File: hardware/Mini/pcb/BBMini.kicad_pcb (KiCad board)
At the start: 2 copper layers, 122 x 88 mm, 31 parts, among them J1 Schurter_CMF1, J2 Display, SW1 SW_Push, U1 ESP8266-12E_NodeMCU_Lolin, U2 MCP3208

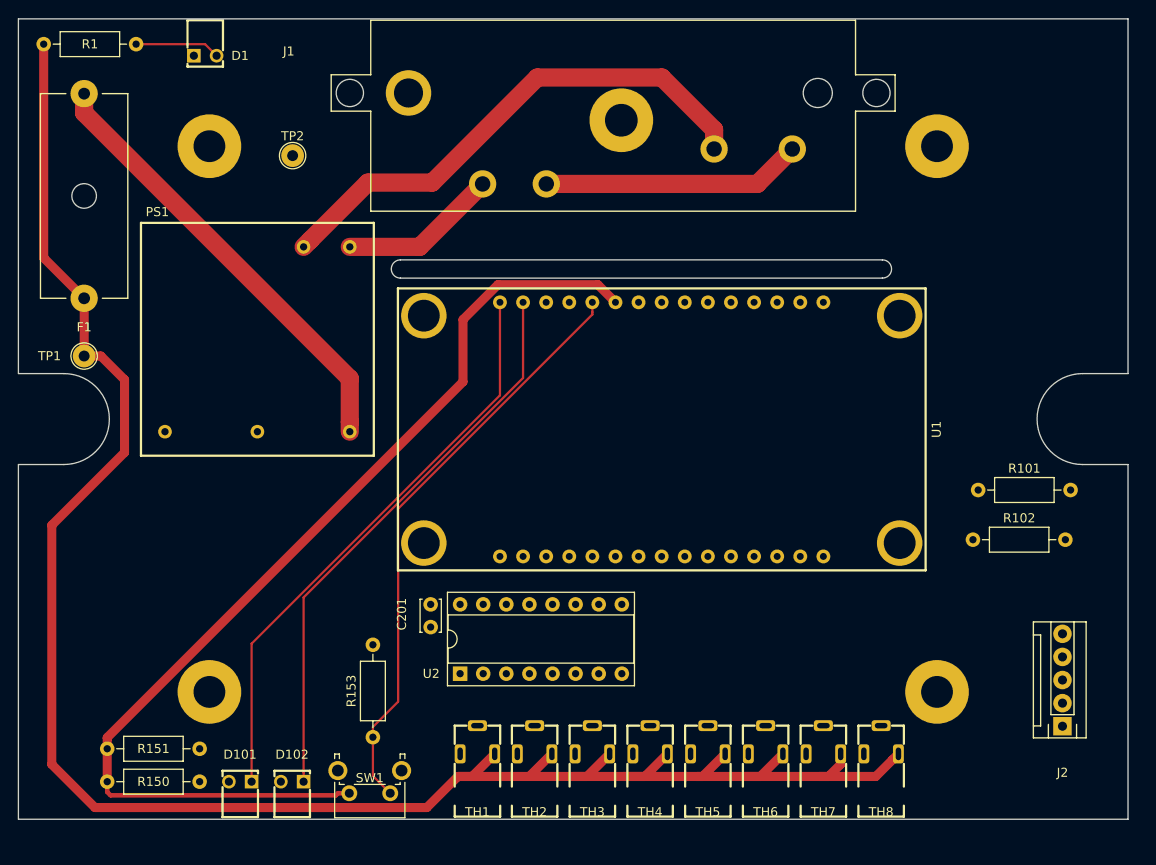
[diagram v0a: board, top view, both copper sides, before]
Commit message: feat: General PCB improvements
add Mini PCB (needs to be redone for RM2015L

Issue #14
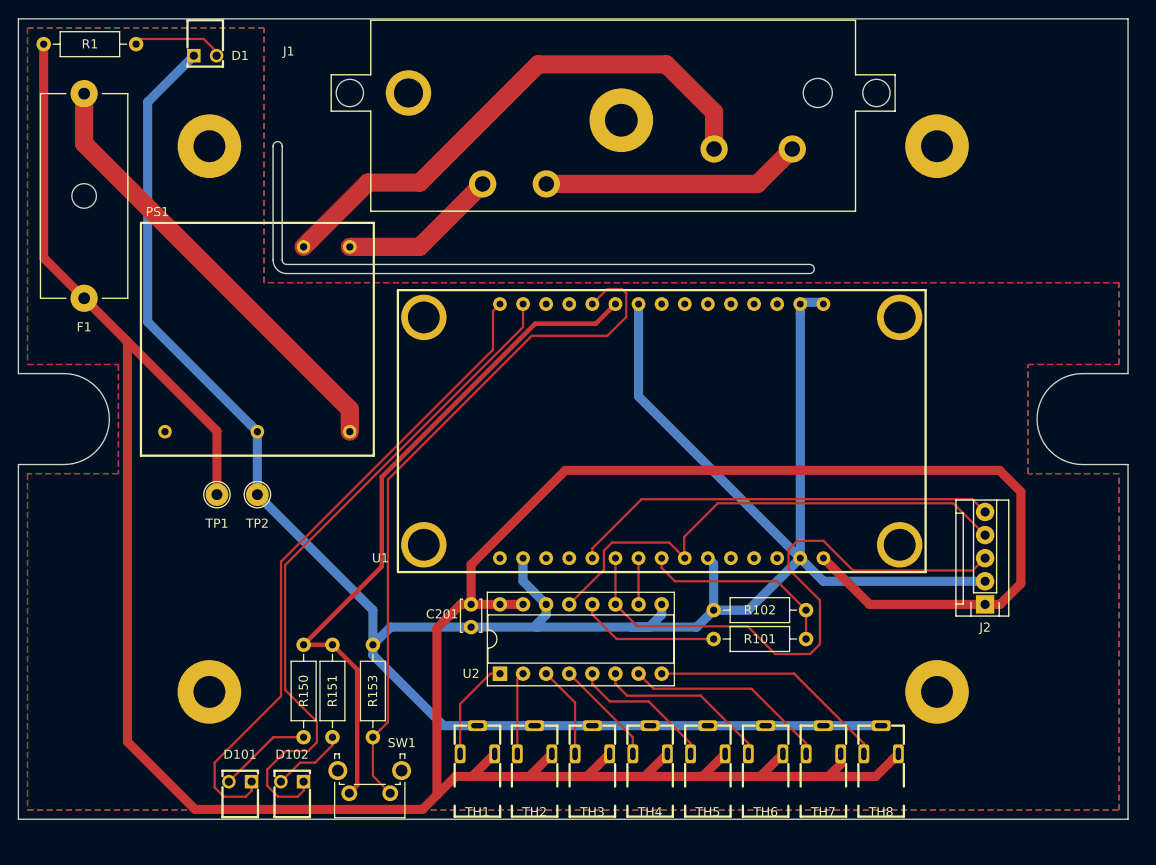
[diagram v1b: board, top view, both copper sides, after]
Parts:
- moved TP2 37.5 mm to (41.3, 67.3)
- moved R151 27.3 mm to (49.5, 83.8), turned to 270 degrees
- moved R150 26.3 mm to (46.4, 83.8), turned to 270 degrees
- moved R101 25.0 mm to (101.6, 83.2), turned to 180 degrees
- moved TP1 21.1 mm to (36.8, 67.3)
- moved R102 19.9 mm to (101.6, 80.0), turned to 180 degrees
- moved J2 15.9 mm to (121.3, 79.4)
- moved C201 4.44 mm to (64.8, 79.4)
- moved U2 4.38 mm to (67.9, 87.0)
- moved U1 0.19 mm to (67.9, 60.3)
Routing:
- net GND: track 0.00 -> 295.4 mm
- net +5V: track 217.7 -> 359.3 mm
- net /Analog/Digital/SPI1: track 0.00 -> 66.0 mm
- net /Analog/Digital/SPI3: track 0.00 -> 55.9 mm
- net /Display/SPI5: track 0.00 -> 47.1 mm
- net +3V3: track 114.2 -> 76.6 mm
- net /Analog/Digital/SIGNAL8: track 0.00 -> 26.6 mm
- net /Analog/Digital/SIGNAL7: track 0.00 -> 22.7 mm
- net /ESP8266/MISO: track 0.00 -> 22.0 mm
- net /Analog/Digital/SIGNAL6: track 0.00 -> 19.6 mm
- net /Analog/Digital/SIGNAL5: track 0.00 -> 15.8 mm
- net /Analog/Digital/SPI2: track 0.00 -> 15.6 mm
- net Net-(D102-Pad1): track 62.7 -> 74.7 mm
- net Net-(R153-Pad1): track 64.8 -> 76.8 mm
- net /Analog/Digital/SIGNAL4: track 0.00 -> 11.7 mm
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- added copper zone on F.Cu, net +5V
- added copper zone on B.Cu, net GND
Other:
- outline, holes or cut-outs redrawn
- net class 3V3 added: clearance 0.3, trace_width 0.5, via_dia 0.8, via_drill 0.4
- net class Large: clearance 0.2 -> 0.5
- net class Medium: clearance 0.2 -> 0.4

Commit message: feat: General PCB improvements
reddo with RM2015L pcb

Issue #14
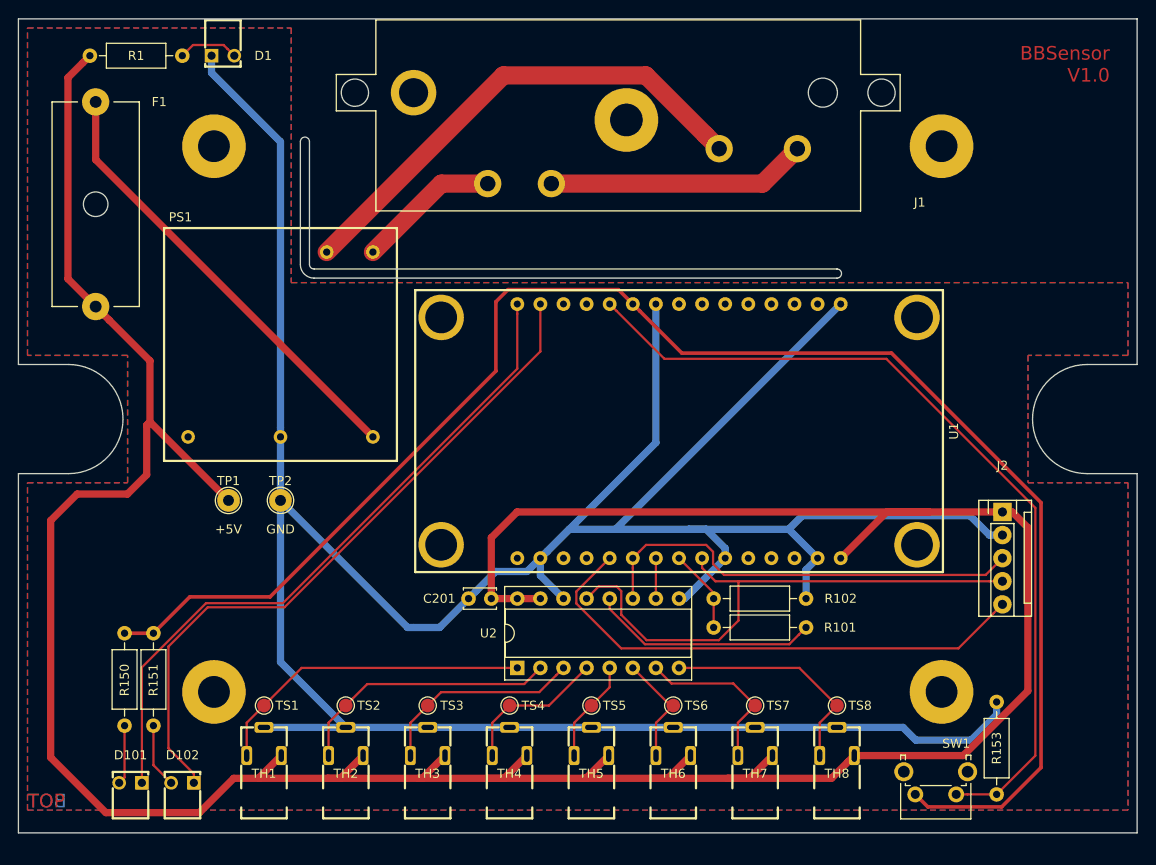
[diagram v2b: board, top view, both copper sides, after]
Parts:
- added TS1: TestPoint, TestPoint:TestPoint_Pad_D1.5mm, F.Cu at (42.0, 90.5)
- added TS2: TestPoint, TestPoint:TestPoint_Pad_D1.5mm, F.Cu at (51.0, 90.5)
- added TS3: TestPoint, TestPoint:TestPoint_Pad_D1.5mm, F.Cu at (60.0, 90.5)
- added TS4: TestPoint, TestPoint:TestPoint_Pad_D1.5mm, F.Cu at (69.0, 90.5)
- added TS5: TestPoint, TestPoint:TestPoint_Pad_D1.5mm, F.Cu at (78.0, 90.5)
- added TS6: TestPoint, TestPoint:TestPoint_Pad_D1.5mm, F.Cu at (87.0, 90.5)
- added TS7: TestPoint, TestPoint:TestPoint_Pad_D1.5mm, F.Cu at (96.0, 90.5)
- added TS8: TestPoint, TestPoint:TestPoint_Pad_D1.5mm, F.Cu at (105.0, 90.5)
- moved R153 68.9 mm to (122.6, 100.3)
- moved SW1 62.2 mm to (118.1, 100.3)
- moved TH1 23.5 mm to (42.0, 102.9)
- moved TH2 20.8 mm to (51.0, 102.9)
- moved R151 19.7 mm to (29.8, 82.5)
- moved R150 19.7 mm to (26.7, 82.5)
- moved TH3 18.1 mm to (60.0, 102.9)
- moved TH4 15.5 mm to (69.0, 102.9)
- moved TH5 12.8 mm to (78.0, 102.9)
- moved D101 12.1 mm to (27.3, 103.0)
- moved D102 12.1 mm to (33.0, 103.0)
- moved J2 10.3 mm to (123.2, 69.2), turned to 0 degrees
- moved R102 10.2 mm to (91.4, 78.7), turned to 0 degrees
- moved R101 10.2 mm to (91.4, 81.9), turned to 0 degrees
- moved TH6 10.2 mm to (87.0, 102.9)
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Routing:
- net +3V3: track 76.6 -> 175.9 mm
- net GND: track 295.4 -> 350.9 mm
- net /Analog/Digital/SIGNAL1: track 11.2 -> 35.9 mm
- net /Analog/Digital/SIGNAL2: track 9.08 -> 29.4 mm
- net /Analog/Digital/SPI1: track 66.0 -> 48.6 mm
- net Net-(R153-Pad1): track 76.8 -> 93.8 mm
- net /ESP8266/MISO: track 22.0 -> 9.20 mm
- net /Analog/Digital/SIGNAL3: track 10.1 -> 22.9 mm
- net /Display/SPI5: track 47.1 -> 57.4 mm
- net /Analog/Digital/SPI2: track 15.6 -> 25.1 mm
- net /Analog/Digital/SIGNAL6: track 19.6 -> 12.5 mm
- net +5V: track 359.3 -> 353.2 mm
- net /Analog/Digital/SPI3: track 55.9 -> 61.1 mm
- net Net-(J1-Pad1): track 59.7 -> 54.5 mm
- net /Analog/Digital/SIGNAL4: track 11.7 -> 16.5 mm
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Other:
- board size 122 x 88 mm -> 123 x 89.5 mm
- net class 3V3: trace_width 0.5 -> 0.4
- net class 5V added: clearance 0.3, trace_width 0.8, via_dia 0.8, via_drill 0.4
- net class AC added: clearance 0.4, trace_width 2, via_dia 0.8, via_drill 0.4
- net class Large removed
- net class Medium removed
- board text added: "+5V"
- board text added: "BBSensor V1.0"
- board text added: "BOT"
- board text added: "GND"
- board text added: "TOP"

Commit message: feat: General PCB improvements
finalize front, need to move mountings

Issue #14
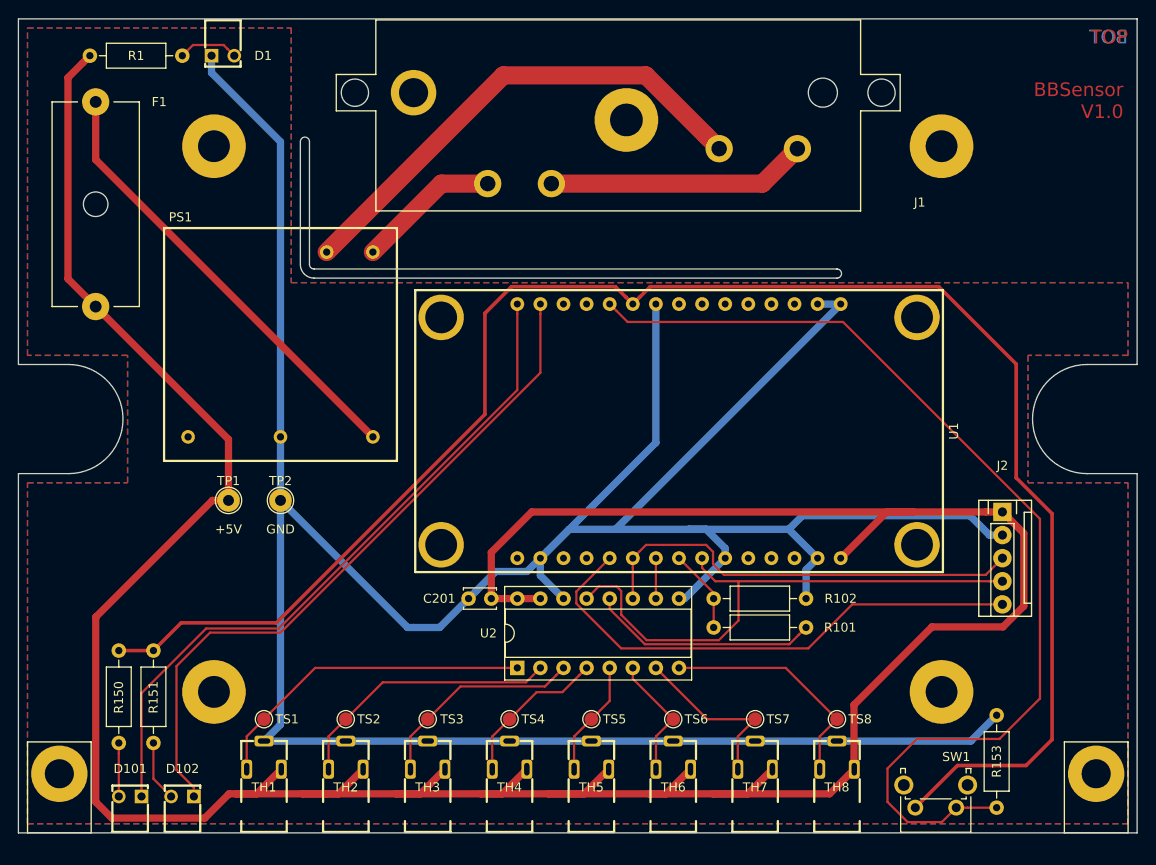
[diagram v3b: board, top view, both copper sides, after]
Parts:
- added ~: Mounting_Bracket_L10_W7_M3, Collection:Mounting_Bracket_L10_W7_M3, F.Cu at (130.0, 104.5)
- added ~: Mounting_Bracket_L10_W7_M3, Collection:Mounting_Bracket_L10_W7_M3, F.Cu at (16.0, 104.5)
- moved R150 2.01 mm to (26.0, 84.5)
- moved R151 1.91 mm to (29.8, 84.5)
- moved D101 1.50 mm to (27.3, 104.5)
- moved D102 1.50 mm to (33.0, 104.5)
- moved TH1 1.50 mm to (42.0, 104.4)
- moved TH2 1.50 mm to (51.0, 104.4)
- moved TH3 1.50 mm to (60.0, 104.4)
- moved TH4 1.50 mm to (69.0, 104.4)
- moved TH5 1.50 mm to (78.0, 104.4)
- moved TH6 1.50 mm to (87.0, 104.4)
- moved TH7 1.50 mm to (96.0, 104.4)
- moved TH8 1.50 mm to (105.0, 104.4)
- moved TS1 1.50 mm to (42.0, 92.0)
- moved TS2 1.50 mm to (51.0, 92.0)
- moved TS3 1.50 mm to (60.0, 92.0)
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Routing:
- net Net-(R153-Pad1): track 93.8 -> 114.0 mm
- net +3V3: track 175.9 -> 187.9 mm
- net +5V: track 353.2 -> 351.6 mm
- net /Analog/Digital/SIGNAL5: track 11.3 -> 12.8 mm
- net /Analog/Digital/SIGNAL6: track 12.5 -> 13.8 mm
- net Net-(D101-Pad1): track 74.7 -> 75.9 mm
- net Net-(D101-Pad2): track 6.53 -> 5.88 mm
- net /Analog/Digital/SIGNAL1: track 35.9 -> 36.5 mm
- net /Analog/Digital/SIGNAL8: track 25.4 -> 26.0 mm
- net /Analog/Digital/SIGNAL4: track 16.5 -> 17.1 mm
- net /Analog/Digital/SIGNAL3: track 22.9 -> 23.6 mm
- net /Analog/Digital/SIGNAL2: track 29.4 -> 30.0 mm
- net /Analog/Digital/SIGNAL7: track 18.9 -> 19.5 mm

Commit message: feat: General PCB improvements
redo pcb with more mountings, fit better to panels

Issue #14
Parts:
- added ~: Mounting_Bracket_L10_W7_M3, Collection:Mounting_Bracket_L10_W7_M3, F.Cu at (134.0, 15.0)
- added ~: Mounting_Bracket_L10_W7_M3, Collection:Mounting_Bracket_L10_W7_M3, F.Cu at (26.0, 15.0)
- J1: footprint Schurter:CMF1 -> Schurter:CMF1_Offset
- moved R150 14.9 mm to (40.6, 81.3), turned to 180 degrees
- moved R151 10.8 mm to (40.6, 84.5), turned to 180 degrees
- moved R1 9.21 mm to (42.2, 19.1), turned to 270 degrees
- moved F1 4.17 mm to (23.5, 50.8)
- moved D101 3.55 mm to (30.5, 106.0)
- moved ~ 3.35 mm to (127.0, 106.0)
- moved ~ 3.35 mm to (19.0, 106.0)
- moved D102 2.94 mm to (35.6, 106.0)
- moved C201 1.50 mm to (67.0, 80.2)
- moved J2 1.50 mm to (123.2, 70.7)
- moved PS1 1.50 mm to (43.8, 52.3)
- moved R101 1.50 mm to (91.4, 83.4)
- moved R102 1.50 mm to (91.4, 80.2)
- moved R153 1.50 mm to (122.6, 103.2)
- moved SW1 1.50 mm to (118.1, 103.2)
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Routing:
- net Net-(D101-Pad2): track 5.88 -> 21.5 mm
- net +3V3: track 187.9 -> 173.7 mm
- net Net-(D102-Pad2): track 6.69 -> 19.1 mm
- net +5V: track 351.6 -> 362.7 mm
- net GND: track 350.8 -> 358.9 mm
- net Net-(D102-Pad1): track 76.0 -> 68.9 mm
- net Net-(J1-Pad1): track 54.5 -> 58.5 mm
- net Net-(D1-Pad2): track 6.69 -> 3.49 mm
- net Net-(F1-Pad2): track 49.5 -> 46.8 mm
- net Net-(D101-Pad1): track 75.9 -> 73.7 mm
- net Net-(J1-Pad3): track 15.7 -> 17.6 mm
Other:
- board size 123 x 89.5 mm -> 123 x 91 mm

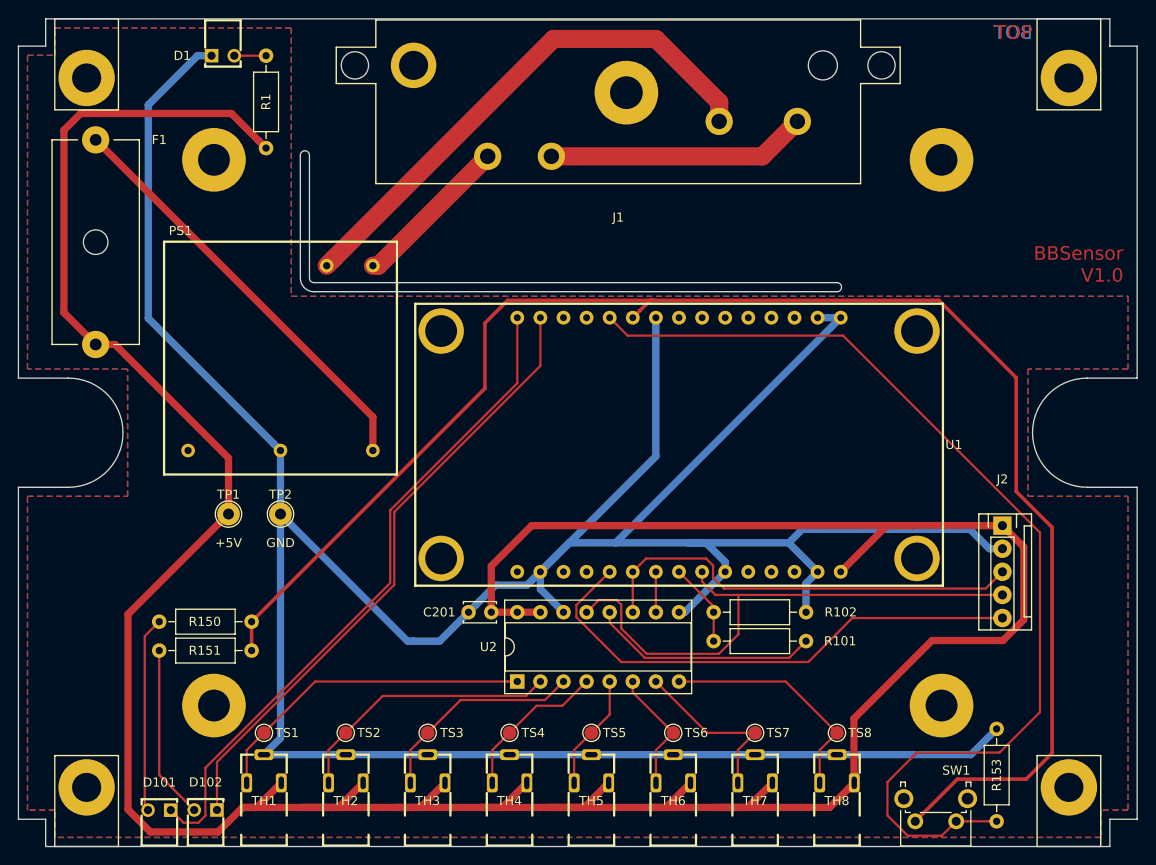
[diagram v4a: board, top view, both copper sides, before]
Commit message: feat: General PCB improvements
fix Display, add BOM

Issue #14
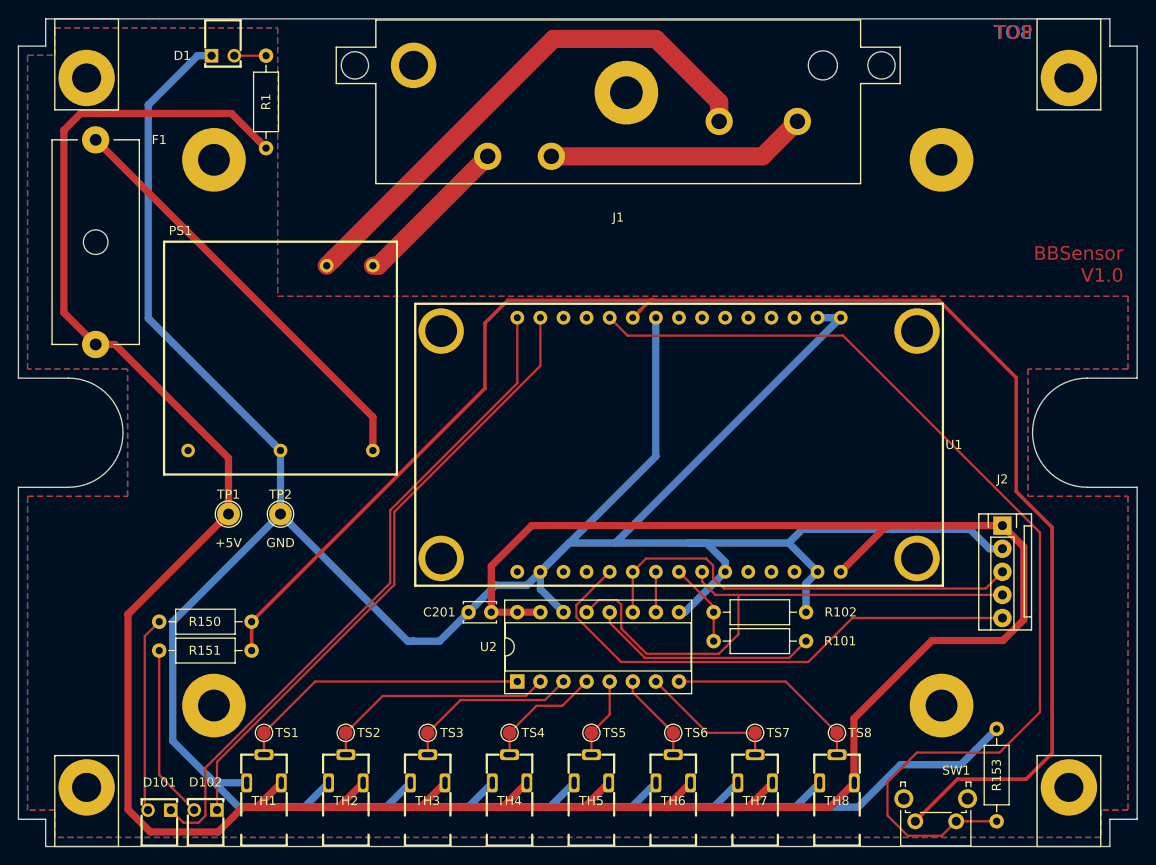
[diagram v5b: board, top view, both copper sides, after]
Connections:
- TH1 pad S: /Analog/Digital/SIGNAL1 -> GND
- TH1 pad T: GND -> /Analog/Digital/SIGNAL1
- TH2 pad S: /Analog/Digital/SIGNAL2 -> GND
- TH2 pad T: GND -> /Analog/Digital/SIGNAL2
- TH3 pad S: /Analog/Digital/SIGNAL3 -> GND
- TH3 pad T: GND -> /Analog/Digital/SIGNAL3
- TH4 pad S: /Analog/Digital/SIGNAL4 -> GND
- TH4 pad T: GND -> /Analog/Digital/SIGNAL4
- TH5 pad S: /Analog/Digital/SIGNAL5 -> GND
- TH5 pad T: GND -> /Analog/Digital/SIGNAL5
- TH6 pad S: /Analog/Digital/SIGNAL6 -> GND
- TH6 pad T: GND -> /Analog/Digital/SIGNAL6
- TH7 pad S: /Analog/Digital/SIGNAL7 -> GND
- TH7 pad T: GND -> /Analog/Digital/SIGNAL7
- TH8 pad S: /Analog/Digital/SIGNAL8 -> GND
- TH8 pad T: GND -> /Analog/Digital/SIGNAL8
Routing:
- net GND: track 358.9 -> 450.0 mm
- net /Analog/Digital/SIGNAL8: track 26.0 -> 22.1 mm
- net /Analog/Digital/SIGNAL7: track 19.5 -> 15.6 mm
- net /Analog/Digital/SIGNAL5: track 12.8 -> 8.87 mm
- net /Analog/Digital/SIGNAL4: track 17.1 -> 13.2 mm
- net /Analog/Digital/SIGNAL6: track 13.8 -> 9.88 mm
- net /Analog/Digital/SIGNAL3: track 23.6 -> 19.7 mm
- net /Analog/Digital/SIGNAL1: track 36.5 -> 32.6 mm
- net /Analog/Digital/SIGNAL2: track 30.0 -> 26.1 mm
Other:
- outline, holes or cut-outs redrawn
